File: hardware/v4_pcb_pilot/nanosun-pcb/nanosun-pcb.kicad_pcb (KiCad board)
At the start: 2 copper layers, 165 x 165 mm, 30 parts

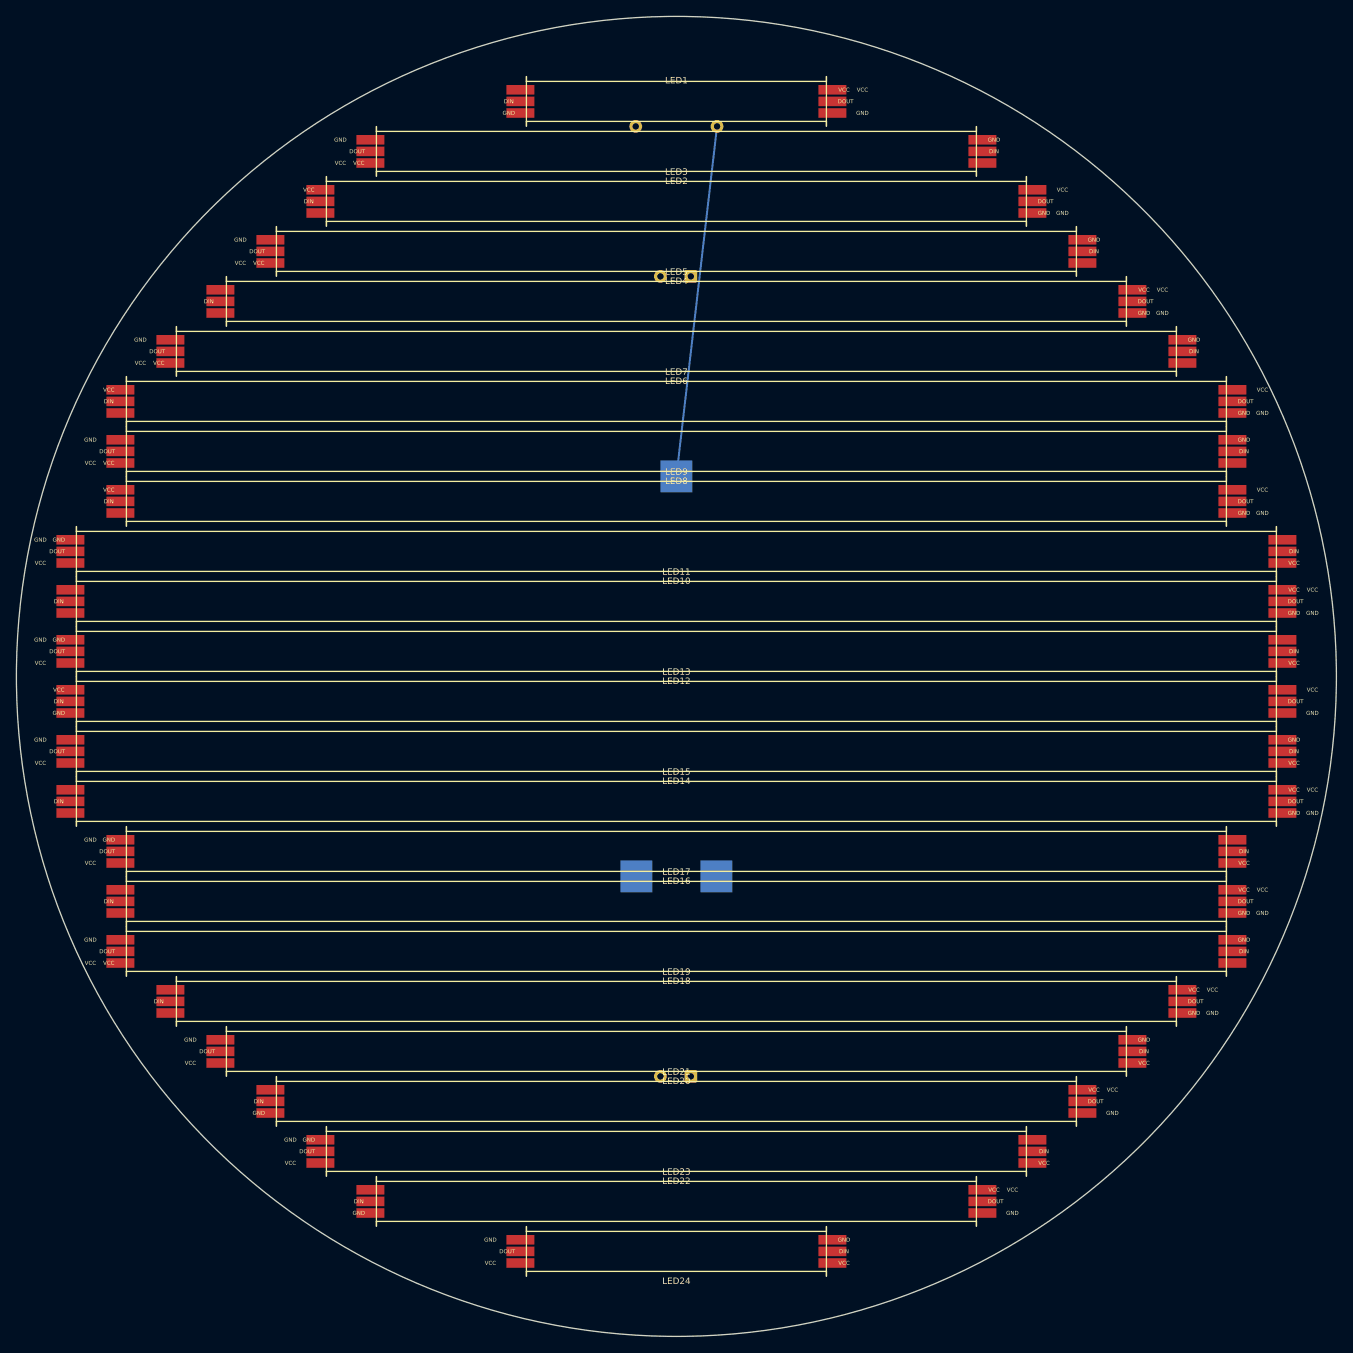
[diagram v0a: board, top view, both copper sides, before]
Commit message: Add MP1584EN buck regulator mounting and remove stray silkscreen rect
Adds a 12V->5V power path on the back side of the PCB:
- New MP1584EN_Module footprint (22x17 mm body, four 3x5 mm corner SMD
  pads on B.Cu) for the generic adjustable buck breakout.
- New schematic symbol with VIN/GND/GND/+5V pins, plus a +5V WireSolderPad
  (J4) so the regulated rail can be tapped off-board. Uses a new local
  power:+5V net driven by the regulator's power_out pin.
- Removes a leftover B.SilkS rectangle that was no longer needed.

ERC: 0 violations.

Co-Authored-By: Claude Opus 4.6 <noreply@anthropic.com>
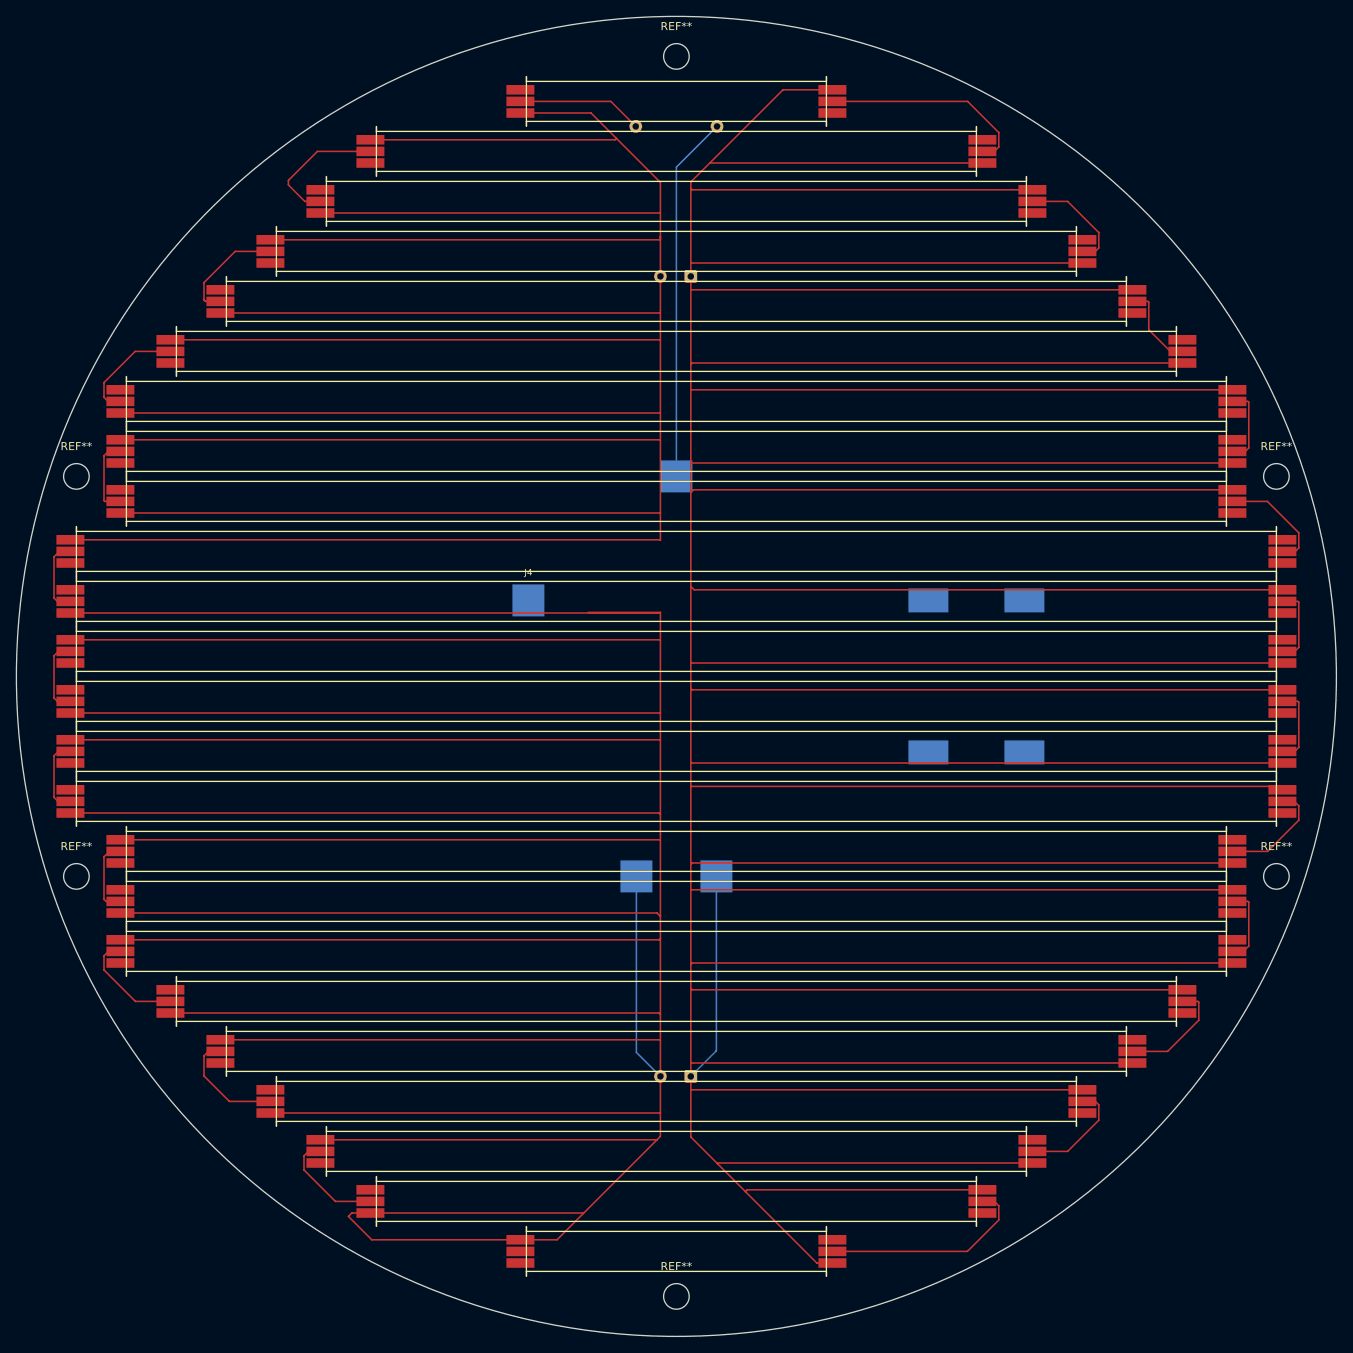
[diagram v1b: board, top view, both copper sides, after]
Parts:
- added J4: +5V, nanosun-pcb:WireSolderPad_1, B.Cu at (131.5, 90.5)
- added REF**: MountingHole_3.2mm_M3_DIN965, MountingHole:MountingHole_3.2mm_M3_DIN965, F.Cu at (75.0, 125.0)
- added REF**: MountingHole_3.2mm_M3_DIN965, MountingHole:MountingHole_3.2mm_M3_DIN965, F.Cu at (150.0, 22.5)
- added REF**: MountingHole_3.2mm_M3_DIN965, MountingHole:MountingHole_3.2mm_M3_DIN965, F.Cu at (225.0, 75.0)
- added REF**: MountingHole_3.2mm_M3_DIN965, MountingHole:MountingHole_3.2mm_M3_DIN965, F.Cu at (150.0, 177.5)
- added REF**: MountingHole_3.2mm_M3_DIN965, MountingHole:MountingHole_3.2mm_M3_DIN965, F.Cu at (75.0, 75.0)
- added REF**: MountingHole_3.2mm_M3_DIN965, MountingHole:MountingHole_3.2mm_M3_DIN965, F.Cu at (225.0, 125.0)
- added U1: MP1584EN_Module, nanosun-pcb:MP1584EN_Module, B.Cu at (187.5, 100.0)
- renumbered 12V to J1, DIN to J2, GND to J3
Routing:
- net GND: track 0.00 -> 1536.0 mm
- net +12V: track 0.00 -> 1446.6 mm
- net Net-(LED1-DOUT): track 0.00 -> 26.5 mm
- net Net-(LED23-DOUT): track 0.00 -> 26.5 mm
- net Net-(LED2-DOUT): track 0.00 -> 17.2 mm
- net Net-(LED1-DIN): track 0.00 -> 15.7 mm
- net Net-(LED20-DOUT): track 0.00 -> 14.4 mm
- net Net-(LED19-DOUT): track 0.00 -> 14.3 mm
- net Net-(LED4-DOUT): track 0.00 -> 14.2 mm
- net Net-(LED21-DOUT): track 0.00 -> 14.1 mm
- net Net-(LED3-DOUT): track 0.00 -> 14.1 mm
- net Net-(LED10-DIN): track 0.00 -> 14.1 mm
- net Net-(LED6-DOUT): track 0.00 -> 14.0 mm
- net Net-(LED15-DOUT): track 0.00 -> 14.0 mm
- net Net-(LED22-DOUT): track 0.00 -> 14.0 mm
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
